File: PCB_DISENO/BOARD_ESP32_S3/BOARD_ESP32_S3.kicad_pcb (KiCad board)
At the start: 2 copper layers, 60.2 x 93.3 mm, 52 parts, among them J1 INPUT_EXT, J2 USB_B_Micro, J3 CON TEST, J4 INPUT_EXT, Q1 Q_NPN_BEC, Q2 Q_NPN_BEC, U1 ESP32-S3-WROOM-1, U2 CH340C, U3 3v3 1A, U5 ACS712

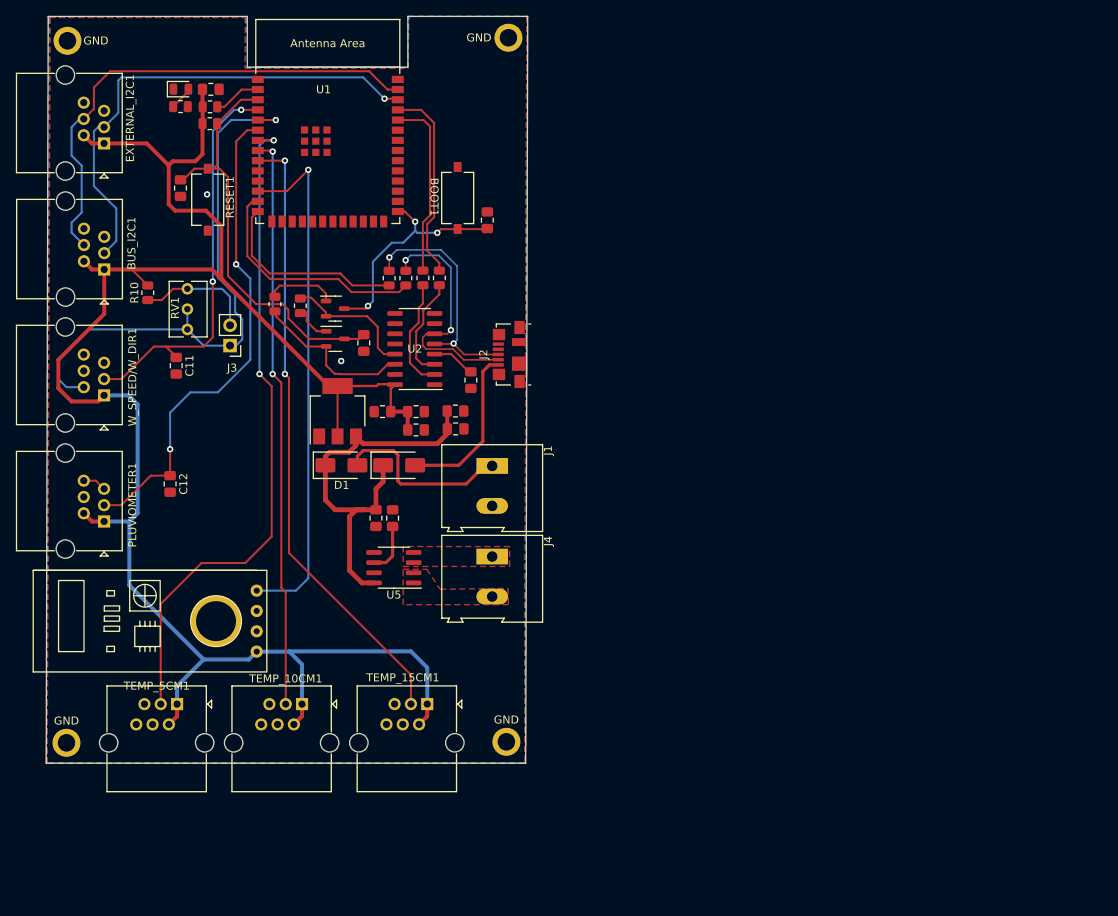
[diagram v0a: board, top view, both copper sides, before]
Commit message: Se agregan elementos de maestria
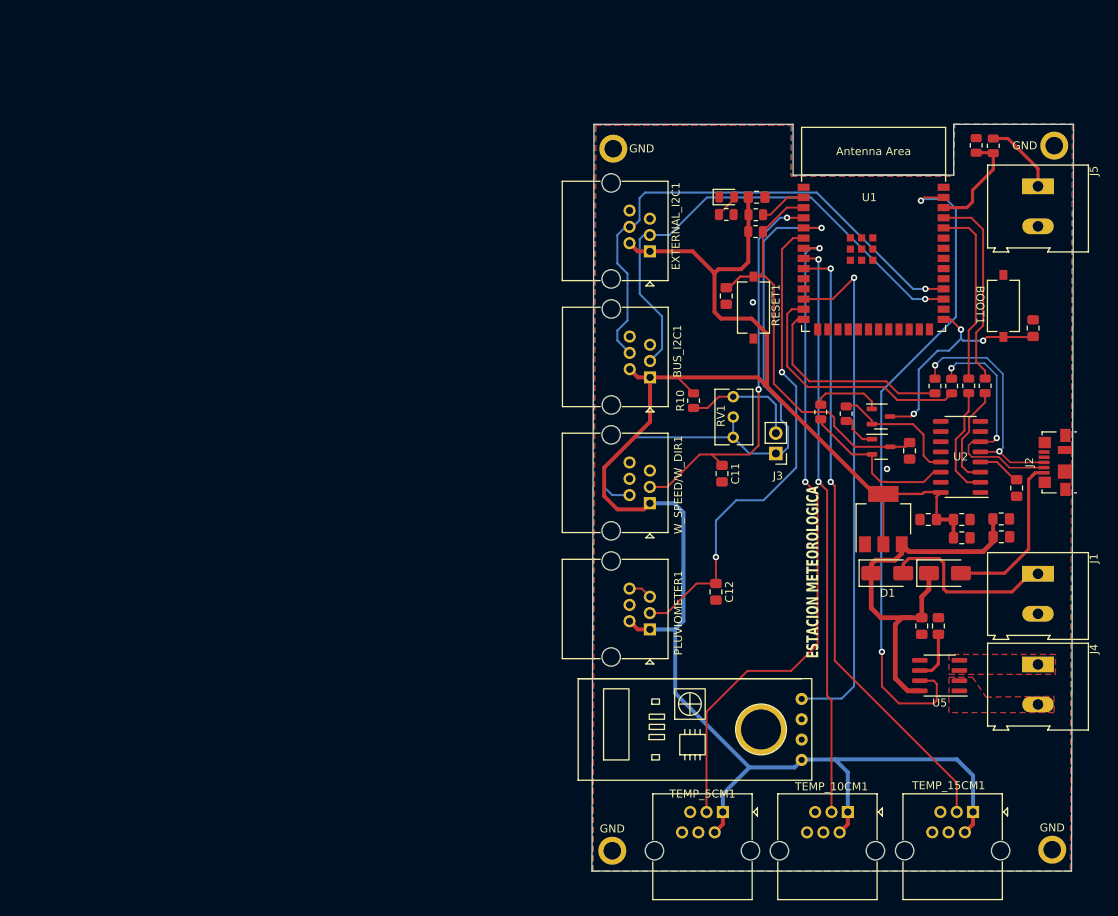
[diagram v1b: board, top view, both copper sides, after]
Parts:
- added J5: INPUT_EXT, TerminalBlock:TerminalBlock_Altech_AK300-2_P5.00mm, F.Cu at (193.4, 41.2)
- added R11: 10K, Resistor_SMD:R_0805_2012Metric, F.Cu at (187.9, 36.1)
- added R12: 10K, Resistor_SMD:R_0805_2012Metric, F.Cu at (185.7, 36.1)
- moved C14 69.5 mm to (181.0, 96.1)
- moved C6 69.5 mm to (192.8, 58.9)
- moved C8 69.5 mm to (158.3, 42.5)
- moved J1 69.5 mm to (193.4, 89.6)
- moved J4 69.5 mm to (193.4, 100.9)
- moved R10 69.5 mm to (150.4, 68.0)
- moved U5 69.5 mm to (181.2, 102.3)
- moved BOOT1 69.5 mm to (189.1, 56.1)
- moved C1 69.5 mm to (190.8, 78.9)
- moved C10 69.5 mm to (154.5, 54.9)
- moved C11 69.5 mm to (153.9, 77.1)
- moved C12 69.5 mm to (153.2, 91.9)
- moved C2 69.5 mm to (188.9, 82.8)
- moved C3 69.5 mm to (188.9, 85.0)
- moved C4 69.5 mm to (183.9, 82.8)
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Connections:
- BUS_I2C1 pad 3: /GPIO02 -> /GPIO36
- BUS_I2C1 pad 4: /GPIO01 -> /GPIO37
- EXTERNAL_I2C1 pad 3: /GPIO02 -> /GPIO36
- EXTERNAL_I2C1 pad 4: /GPIO01 -> /GPIO37
- U5 pad 7: unconnected-(U5-VIOUT-Pad7) -> /GPIO01
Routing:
- net /GPIO37: track 0.00 -> 66.0 mm, vias 0 -> 1
- net /GPIO36: track 0.00 -> 62.4 mm, vias 0 -> 1
- net /GPIO02: track 61.3 -> 13.6 mm, vias 1 -> 0
- net /GPIO01: track 62.6 -> 83.8 mm, vias 0 -> 2
- net Net-(J5-Pin_1): track 0.00 -> 10.5 mm
- net /GPIO19: track 29.8 -> 31.5 mm
- net /GPIO20: track 24.5 -> 25.9 mm
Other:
- board text added: "ESTACION METEOROLOGICA"
